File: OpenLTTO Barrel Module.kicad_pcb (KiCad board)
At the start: 2 copper layers, 25 x 50 mm, 16 parts, among them Q1 IRLML6244, Q2 IRLML6244, Q3 IRLML6244, U1 TSOP4138

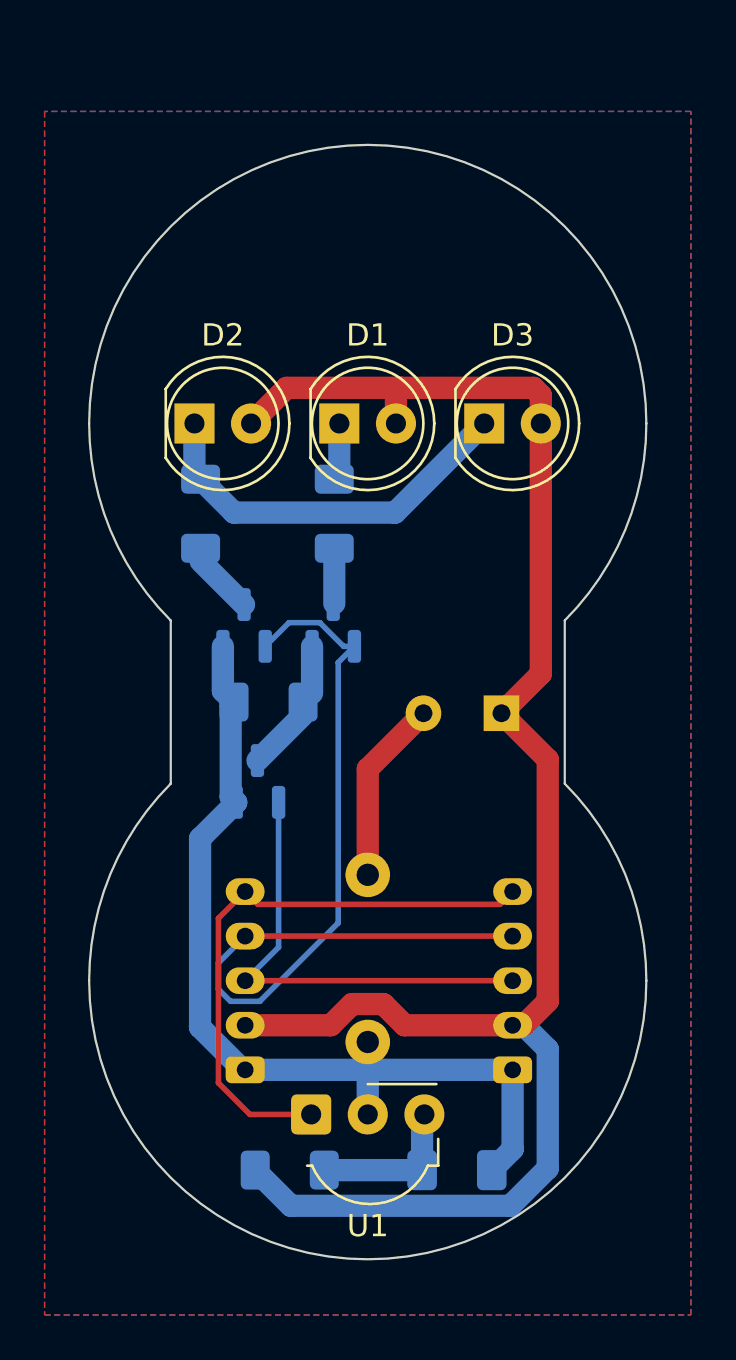
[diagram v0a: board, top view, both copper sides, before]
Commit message: Updated module to allow 3mm gap between optical elements (for easier assembly design)
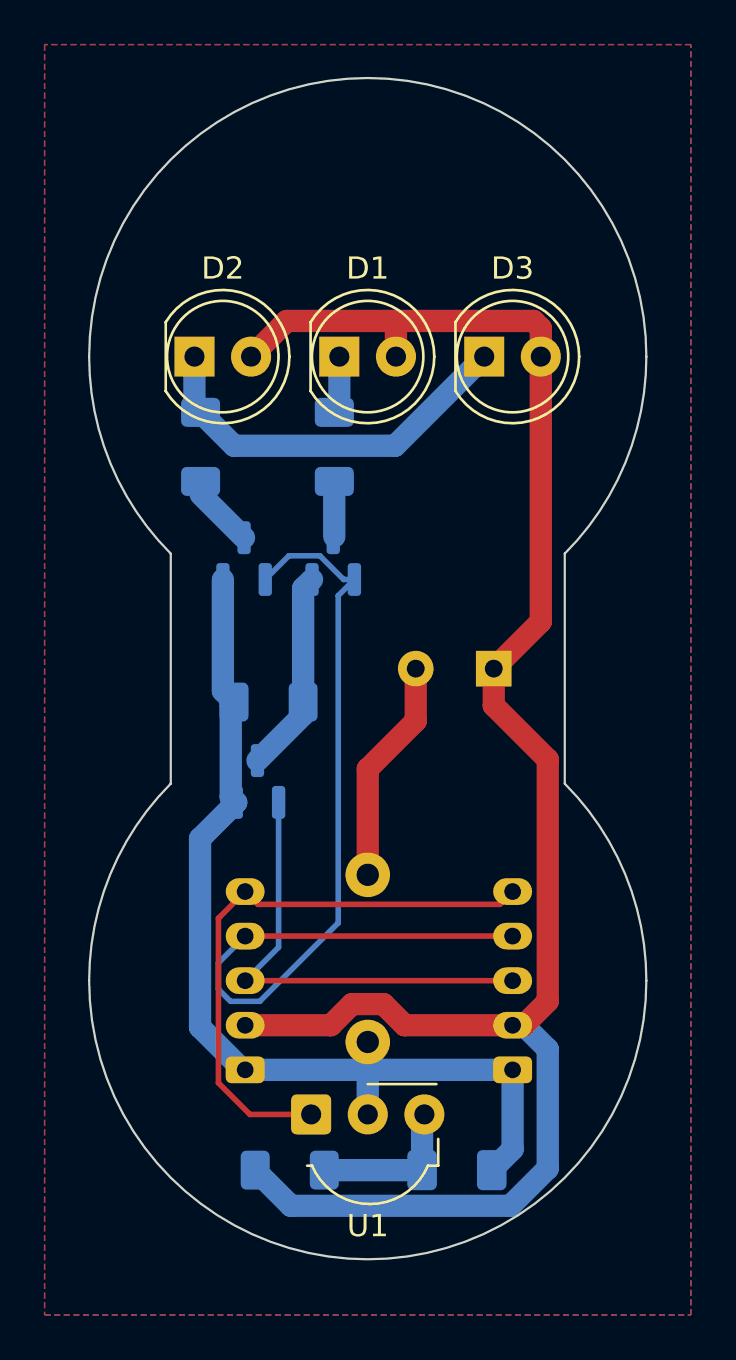
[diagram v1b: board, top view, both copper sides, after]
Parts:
- moved D1 3.00 mm to (166.2, 83.0)
- moved D2 3.00 mm to (159.7, 83.0)
- moved D3 3.00 mm to (172.7, 83.0)
- moved Q2 3.00 mm to (165.9, 92.1)
- moved Q3 3.00 mm to (161.9, 92.1)
- moved R2 3.00 mm to (166.0, 87.0)
- moved R4 3.00 mm to (160.0, 87.0)
- moved C1 2.03 mm to (173.2, 97.0)
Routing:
- net Net-(Q1-D): track 6.14 -> 10.3 mm
- net +5V: track 80.9 -> 84.2 mm
- net GND: track 41.1 -> 44.1 mm
- net /IR_TX: track 39.5 -> 42.5 mm
- net Net-(C1-Pad2): track 8.29 -> 10.1 mm
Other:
- board size 25 x 50 mm -> 25 x 53 mm

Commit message: Minor change, shifted ballast cap to make room for internal baffle on optical assembly
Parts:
- moved C1 2.00 mm to (173.2, 99.0)
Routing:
- net Net-(C1-Pad2): track 10.1 -> 8.82 mm
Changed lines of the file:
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@@
   )
   (footprint "Capacitor_THT:CP_Radial_D8.0mm_P3.50mm" (layer "B.Cu")
-    (at 173.152651 97 180)
+    (at 173.152651 99 180)
     (descr "CP, Radial series, Radial, pin pitch=3.50mm, , diameter=8mm, Electrolytic Capacitor")
     (tags "CP Radial series Radial pin pitch 3.50mm  diameter 8mm Electrolytic Capacitor")
@@
   (gr_arc (start 180 111) (mid 167.5 123.5) (end 155 111)
     (stroke (width 0.1) (type default)) (layer "Edge.Cuts"))
-  (segment (start 175.265 94.887651) (end 175.265 83) (width 1) (layer "F.Cu") (net 1))
+  (segment (start 175.265 98.235) (end 174.5 99) (width 1) (layer "F.Cu") (net 1))
+  (segment (start 175.265 83) (end 175.265 98.235) (width 1) (layer "F.Cu") (net 1))
   (segment (start 169.154164 113) (end 174 113) (width 1) (layer "F.Cu") (net 1))
   (segment (start 175.265 83) (end 175.265 81.727208) (width 1) (layer "F.Cu") (net 1))
-  (segment (start 174.5 113) (end 174 113) (width 1) (layer "F.Cu") (net 1))
+  (segment (start 175.575 100.075) (end 174.5 99) (width 1) (layer "F.Cu") (net 1))
+  (segment (start 175.575 111.925) (end 175.575 100.075) (width 1) (layer "F.Cu") (net 1))
   (segment (start 162 113) (end 165.845836 113) (width 1) (layer "F.Cu") (net 1))
   (segment (start 166.795836 112.05) (end 168.204164 112.05) (width 1) (layer "F.Cu") (net 1))
   (segment (start 175.265 81.727208) (end 174.937792 81.4) (width 1) (layer "F.Cu") (net 1))
-  (segment (start 175.575 111.925) (end 174.5 113) (width 1) (layer "F.Cu") (net 1))
+  (segment (start 174.5 113) (end 175.575 111.925) (width 1) (layer "F.Cu") (net 1))
   (segment (start 168.765 81.635) (end 169 81.4) (width 1) (layer "F.Cu") (net 1))
-  (segment (start 175.575 101.075) (end 175.575 111.925) (width 1) (layer "F.Cu") (net 1))
   (segment (start 169 81.4) (end 163.865 81.4) (width 1) (layer "F.Cu") (net 1))
+  (segment (start 174.5 99) (end 173.152651 99) (width 1) (layer "F.Cu") (net 1))
   (segment (start 165.845836 113) (end 166.795836 112.05) (width 1) (layer "F.Cu") (net 1))
   (segment (start 163.865 81.4) (end 162.265 83) (width 1) (layer "F.Cu") (net 1))
   (segment (start 174.937792 81.4) (end 169 81.4) (width 1) (layer "F.Cu") (net 1))
-  (segment (start 173.152651 98.652651) (end 173.152651 97) (width 1) (layer "F.Cu") (net 1))
-  (segment (start 173.152651 97) (end 175.265 94.887651) (width 1) (layer "F.Cu") (net 1))
+  (segment (start 174 113) (end 174.5 113) (width 1) (layer "F.Cu") (net 1))
   (segment (start 168.204164 112.05) (end 169.154164 113) (width 1) (layer "F.Cu") (net 1))
-  (segment (start 175.575 101.075) (end 173.152651 98.652651) (width 1) (layer "F.Cu") (net 1))
   (segment (start 168.765 83) (end 168.765 81.635) (width 1) (layer "F.Cu") (net 1))
   (segment (start 162.45 119.5) (end 164.05 121.1) (width 1) (layer "B.Cu") (net 1))
@@
   (segment (start 175.575 114.075) (end 174.5 113) (width 1) (layer "B.Cu") (net 1))
   (segment (start 175.575 119.425) (end 175.575 114.075) (width 1) (layer "B.Cu") (net 1))
-  (segment (start 167.5 106.25) (end 167.5 101.5) (width 1) (layer "F.Cu") (net 2))
-  (segment (start 167.5 101.5) (end 169.652651 99.347349) (width 1) (layer "F.Cu") (net 2))
-  (segment (start 169.652651 99.347349) (end 169.652651 97) (width 1) (layer "F.Cu") (net 2))
+  (segment (start 167.5 100) (end 168.5 99) (width 1) (layer "F.Cu") (net 2))
+  (segment (start 167.5 106.25) (end 167.5 100) (width 1) (layer "F.Cu") (net 2))
+  (segment (start 168.5 99) (end 169.652651 99) (width 1) (layer "F.Cu") (net 2))
   (segment (start 166.225 85.275) (end 166.225 83) (width 1) (layer "B.Cu") (net 3))
   (segment (start 166 85.5) (end 166.225 85.275) (width 0.25) (layer "B.Cu") (net 3))
